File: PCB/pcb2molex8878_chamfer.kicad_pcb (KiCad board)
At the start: 2 copper layers, 16 x 38.2 mm, 2 parts

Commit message: fix pocket dims to account for fitment clearance
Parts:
- gave numbers to parts that had none: 1
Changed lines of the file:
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@@
     (descr "Castellated edge contacts to fit Molex 8878 Socket")
     (solder_mask_margin -0.28)
-    (fp_text reference J? (at -1.5 0 -90) (layer Dwgs.User) hide
+    (fp_text reference m? (at -1.5 0 -90) (layer Dwgs.User) hide
       (effects (font (size 1.2065 1.2065) (thickness 0.127)) (justify left bottom))
     )
@@
       (effects (font (size 1.2065 1.2065) (thickness 0.1016)) (justify left bottom))
     )
+    (fp_line (start 7.2 18.3) (end -7.2 18.3) (layer Dwgs.User) (width 0.01))
+    (fp_line (start 7.2 -18.3) (end 7.2 18.3) (layer Dwgs.User) (width 0.01))
+    (fp_line (start -7.2 -18.3) (end 7.2 -18.3) (layer Dwgs.User) (width 0.01))
+    (fp_line (start -7.2 18.3) (end -7.2 -18.3) (layer Dwgs.User) (width 0.01))
     (fp_text user "backside pocket" (at -4.6 2.85) (layer Dwgs.User)
       (effects (font (size 0.2 0.2) (thickness 0.01)))
     )
-    (fp_text user "36.7 x 14.5 x 1.6" (at -4.6 3.2) (layer Dwgs.User)
+    (fp_text user "36.6 x 14.4 x 1.6" (at -4.6 3.2) (layer Dwgs.User)
       (effects (font (size 0.2 0.2) (thickness 0.01)))
     )
-    (fp_line (start -7.25 3) (end -6 3) (layer Dwgs.User) (width 0.01))
-    (fp_line (start -7.25 3) (end -6.75 3.5) (layer Dwgs.User) (width 0.01))
-    (fp_line (start -7.25 3) (end -6.75 2.5) (layer Dwgs.User) (width 0.01))
-    (fp_line (start 7.25 -18.35) (end 7.25 18.35) (layer Dwgs.User) (width 0.01))
-    (fp_line (start -7.25 -18.35) (end -7.25 18.35) (layer Dwgs.User) (width 0.01))
-    (fp_line (start 7.25 -18.35) (end -7.25 -18.35) (layer Dwgs.User) (width 0.01))
-    (fp_line (start 7.25 18.35) (end -7.25 18.35) (layer Dwgs.User) (width 0.01))
+    (fp_line (start -7.2 3) (end -5.95 3) (layer Dwgs.User) (width 0.01))
+    (fp_line (start -7.2 3) (end -6.7 3.5) (layer Dwgs.User) (width 0.01))
+    (fp_line (start -7.2 3) (end -6.7 2.5) (layer Dwgs.User) (width 0.01))
     (fp_line (start -8 -17.3) (end -6.2 -19.1) (layer Eco2.User) (width 0.01))
     (fp_line (start -8 19.1) (end -8 -17.3) (layer Eco2.User) (width 0.01))

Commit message: show retainer wedges on pcb drawings. add daughterboard in carrier model.
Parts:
- gave numbers to parts that had none: 2
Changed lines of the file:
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@@
     (diff_pair_gap 0.254)
-  )
-  (module 000_LOCAL:pcb2molex8878_chamfer (layer Top)
-    (at 147.2184 99.187)
-    (descr "Castellated edge contacts to fit Molex 8878 Socket")
-    (solder_mask_margin -0.28)
-    (fp_text reference m? (at -1.5 0 -90) (layer Dwgs.User) hide
-      (effects (font (size 1.2065 1.2065) (thickness 0.127)) (justify left bottom))
-    )
-    (fp_text value pcb2molex8878_chamfer (at 2.23 -9.45 -90) (layer F.Fab) hide
-      (effects (font (size 1.2065 1.2065) (thickness 0.1016)) (justify left bottom))
-    )
-    (fp_line (start 7.2 18.3) (end -7.2 18.3) (layer Dwgs.User) (width 0.01))
-    (fp_line (start 7.2 -18.3) (end 7.2 18.3) (layer Dwgs.User) (width 0.01))
-    (fp_line (start -7.2 -18.3) (end 7.2 -18.3) (layer Dwgs.User) (width 0.01))
-    (fp_line (start -7.2 18.3) (end -7.2 -18.3) (layer Dwgs.User) (width 0.01))
-    (fp_text user "backside pocket" (at -4.6 2.85) (layer Dwgs.User)
-      (effects (font (size 0.2 0.2) (thickness 0.01)))
-    )
-    (fp_text user "36.6 x 14.4 x 1.6" (at -4.6 3.2) (layer Dwgs.User)
-      (effects (font (size 0.2 0.2) (thickness 0.01)))
-    )
-    (fp_line (start -7.2 3) (end -5.95 3) (layer Dwgs.User) (width 0.01))
-    (fp_line (start -7.2 3) (end -6.7 3.5) (layer Dwgs.User) (width 0.01))
-    (fp_line (start -7.2 3) (end -6.7 2.5) (layer Dwgs.User) (width 0.01))
-    (fp_line (start -8 -17.3) (end -6.2 -19.1) (layer Eco2.User) (width 0.01))
-    (fp_line (start -8 19.1) (end -8 -17.3) (layer Eco2.User) (width 0.01))
-    (fp_line (start 8 19.1) (end -8 19.1) (layer Eco2.User) (width 0.01))
-    (fp_line (start 8 -19.1) (end 8 19.1) (layer Eco2.User) (width 0.01))
-    (fp_line (start -6.2 -19.1) (end 8 -19.1) (layer Eco2.User) (width 0.01))
-    (fp_line (start -8 -19.1) (end -6.2 -19.1) (layer Dwgs.User) (width 0.01))
-    (fp_line (start -8 -19.1) (end -8 -17.3) (layer Dwgs.User) (width 0.01))
-    (fp_line (start -8 -19.1) (end 8 19.1) (layer Dwgs.User) (width 0.01))
-    (fp_line (start -8 19.1) (end 8 -19.1) (layer Dwgs.User) (width 0.01))
-    (fp_text user "Eco2.User is Edge.Cuts for use with \"pcb2molex8878_chamfer\" carrier." (at -0.05 13.65) (layer Eco2.User)
-      (effects (font (size 0.2 0.2) (thickness 0.01)))
-    )
-    (model ${KIPRJMOD}/000_LOCAL.pretty/3d/pcb2molex8878_chamfer.step
-      (offset (xyz 0 0 -0.4))
-      (scale (xyz 1 1 1))
-      (rotate (xyz 0 0 90))
-    )
   )
   (module 000_LOCAL:pcb2molex8878 locked (layer Top)
@@
     (descr "Castellated edge contacts to fit Molex 8878 Socket")
     (solder_mask_margin -0.28)
-    (fp_text reference J? (at -0.9906 -0.9906 -90) (layer Dwgs.User) hide
+    (fp_text reference contacts1 (at -0.9906 -0.9906 -90) (layer Dwgs.User) hide
       (effects (font (size 1.2065 1.2065) (thickness 0.127)) (justify left bottom))
     )
@@
       (solder_mask_margin -0.19))
   )
+  (module 000_LOCAL:pcb2molex8878_chamfer (layer Top)
+    (at 147.2184 99.187)
+    (descr "Castellated edge contacts to fit Molex 8878 Socket")
+    (solder_mask_margin -0.28)
+    (fp_text reference carrier1 (at -1.5 0 -90) (layer Dwgs.User) hide
+      (effects (font (size 1.2065 1.2065) (thickness 0.127)) (justify left bottom))
+    )
+    (fp_text value pcb2molex8878_chamfer (at 2.23 -9.45 -90) (layer F.Fab) hide
+      (effects (font (size 1.2065 1.2065) (thickness 0.1016)) (justify left bottom))
+    )
+    (fp_text user "10.0 x 1.0 retainer wedges on top surface" (at 0.6 -17.3) (layer Dwgs.User)
+      (effects (font (size 0.2 0.2) (thickness 0.01)))
+    )
+    (fp_line (start -3 -18.1) (end -2.8 -17.9) (layer Dwgs.User) (width 0.01))
+    (fp_line (start -3.2 -17.9) (end -3 -18.1) (layer Dwgs.User) (width 0.01))
+    (fp_line (start -3 -18.1) (end -3.2 -17.9) (layer Dwgs.User) (width 0.01))
+    (fp_line (start -3 -18.1) (end -3 -17.2) (layer Dwgs.User) (width 0.01))
+    (fp_line (start 5 19.1) (end -5 19.1) (layer Dwgs.User) (width 0.01))
+    (fp_line (start 5 18.1) (end 5 19.1) (layer Dwgs.User) (width 0.01))
+    (fp_line (start -5 18.1) (end 5 18.1) (layer Dwgs.User) (width 0.01))
+    (fp_line (start -5 19.1) (end -5 18.1) (layer Dwgs.User) (width 0.01))
+    (fp_line (start 5 -19.1) (end -5 -19.1) (layer Dwgs.User) (width 0.01))
+    (fp_line (start 5 -18.1) (end 5 -19.1) (layer Dwgs.User) (width 0.01))
+    (fp_line (start -5 -18.1) (end 5 -18.1) (layer Dwgs.User) (width 0.01))
+    (fp_line (start -5 -19.1) (end -5 -18.1) (layer Dwgs.User) (width 0.01))
+    (fp_line (start 7.2 18.3) (end -7.2 18.3) (layer Dwgs.User) (width 0.01))
+    (fp_line (start 7.2 -18.3) (end 7.2 18.3) (layer Dwgs.User) (width 0.01))
+    (fp_line (start -7.2 -18.3) (end 7.2 -18.3) (layer Dwgs.User) (width 0.01))
+    (fp_line (start -7.2 18.3) (end -7.2 -18.3) (layer Dwgs.User) (width 0.01))
+    (fp_text user "backside pocket" (at -4.6 2.85) (layer Dwgs.User)
+      (effects (font (size 0.2 0.2) (thickness 0.01)))
+    )
+    (fp_text user "36.6 x 14.4 x 1.6" (at -4.6 3.2) (layer Dwgs.User)
+      (effects (font (size 0.2 0.2) (thickness 0.01)))
+    )
+    (fp_line (start -7.2 3) (end -5.95 3) (layer Dwgs.User) (width 0.01))
+    (fp_line (start -7.2 3) (end -6.7 3.5) (layer Dwgs.User) (width 0.01))
+    (fp_line (start -7.2 3) (end -6.7 2.5) (layer Dwgs.User) (width 0.01))
+    (fp_line (start -8 -17.3) (end -6.2 -19.1) (layer Eco2.User) (width 0.01))
+    (fp_line (start -8 19.1) (end -8 -17.3) (layer Eco2.User) (width 0.01))
+    (fp_line (start 8 19.1) (end -8 19.1) (layer Eco2.User) (width 0.01))
+    (fp_line (start 8 -19.1) (end 8 19.1) (layer Eco2.User) (width 0.01))
+    (fp_line (start -6.2 -19.1) (end 8 -19.1) (layer Eco2.User) (width 0.01))
+    (fp_line (start -8 -19.1) (end -6.2 -19.1) (layer Dwgs.User) (width 0.01))
+    (fp_line (start -8 -19.1) (end -8 -17.3) (layer Dwgs.User) (width 0.01))
+    (fp_line (start -8 -19.1) (end 8 19.1) (layer Dwgs.User) (width 0.01))
+    (fp_line (start -8 19.1) (end 8 -19.1) (layer Dwgs.User) (width 0.01))
+    (fp_text user "Eco2.User is Edge.Cuts for use with \"pcb2molex8878_chamfer\" carrier." (at -0.05 13.65) (layer Eco2.User)
+      (effects (font (size 0.2 0.2) (thickness 0.01)))
+    )
+    (model ${KIPRJMOD}/000_LOCAL.pretty/3d/pcb2molex8878_chamfer.step
+      (offset (xyz 0 0 -0.4))
+      (scale (xyz 1 1 1))
+      (rotate (xyz 0 0 90))
+    )
+  )
   (gr_line (start 139.2184 81.887) (end 139.2184 118.287) (layer Edge.Cuts) (width 0.0254))

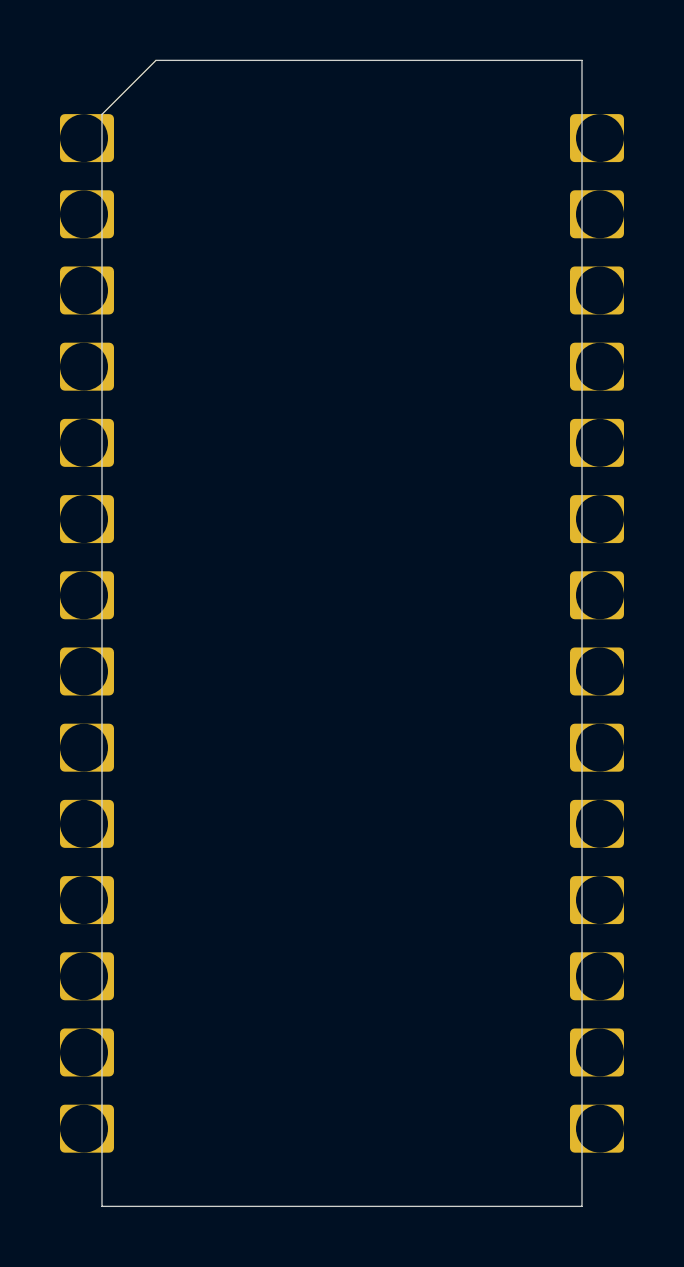
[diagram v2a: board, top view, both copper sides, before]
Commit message: reduce outside X Y dims by 0.1mm for 3d printing variability
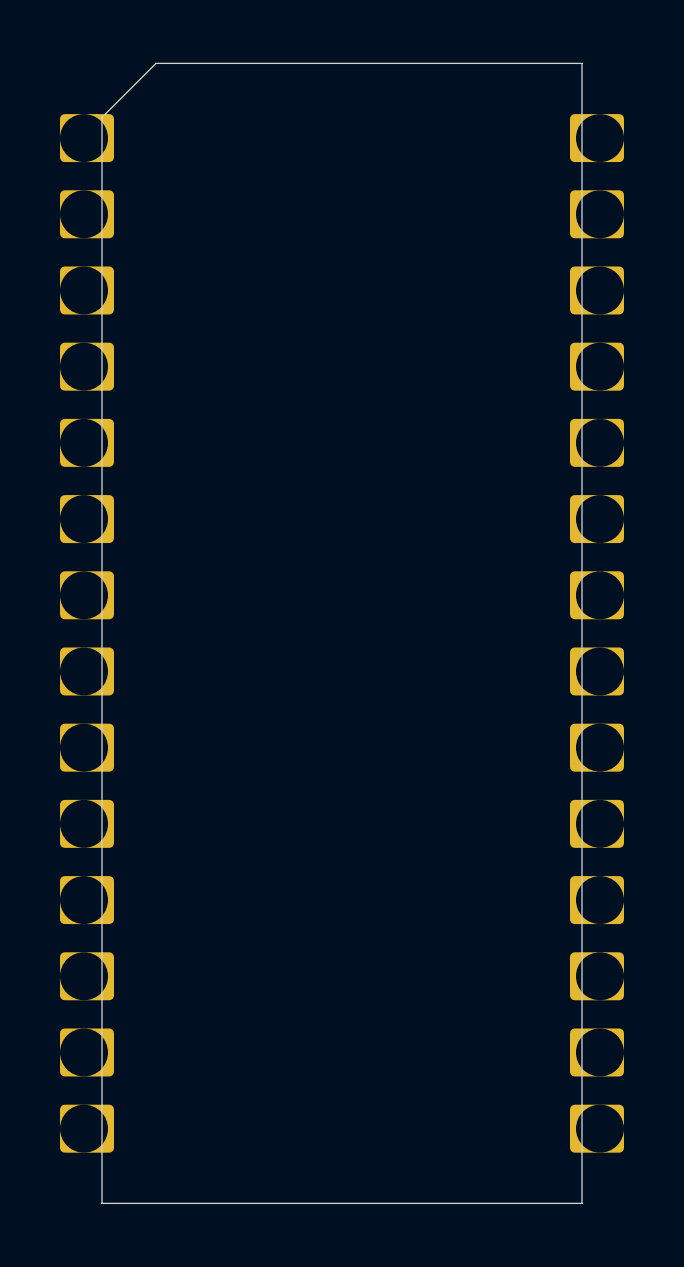
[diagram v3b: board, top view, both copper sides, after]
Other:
- board size 16 x 38.2 mm -> 16 x 38 mm
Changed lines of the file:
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@@
-(kicad_pcb (version 20171130) (host pcbnew 5.1.4-e60b266~84~ubuntu19.04.1)
+(kicad_pcb (version 20171130) (host pcbnew 5.1.5-52549c5~84~ubuntu19.04.1)
   (general
     (thickness 1.6)
@@
     (diff_pair_gap 0.254)
   )
+  (module 000_LOCAL:pcb2molex8878_chamfer (layer Top)
+    (at 147.2184 99.187)
+    (descr "Castellated edge contacts to fit Molex 8878 Socket")
+    (solder_mask_margin -0.28)
+    (fp_text reference carrier1 (at -1.5 0 -90) (layer Dwgs.User) hide
+      (effects (font (size 1.2065 1.2065) (thickness 0.127)) (justify left bottom))
+    )
+    (fp_text value pcb2molex8878_chamfer (at 2.23 -9.45 -90) (layer F.Fab) hide
+      (effects (font (size 1.2065 1.2065) (thickness 0.1016)) (justify left bottom))
+    )
+    (fp_line (start -8 19) (end -8 -17.2) (layer Eco2.User) (width 0.01))
+    (fp_text user "10.0 x 1.0 retainer wedges on top surface" (at 0.6 -17.3) (layer Dwgs.User)
+      (effects (font (size 0.2 0.2) (thickness 0.01)))
+    )
+    (fp_line (start -3 -18) (end -2.8 -17.8) (layer Dwgs.User) (width 0.01))
+    (fp_line (start -3.2 -17.8) (end -3 -18) (layer Dwgs.User) (width 0.01))
+    (fp_line (start -3 -18) (end -3.2 -17.8) (layer Dwgs.User) (width 0.01))
+    (fp_line (start -3 -18) (end -3 -17.1) (layer Dwgs.User) (width 0.01))
+    (fp_line (start 5 19) (end -5 19) (layer Dwgs.User) (width 0.01))
+    (fp_line (start 5 18) (end 5 19) (layer Dwgs.User) (width 0.01))
+    (fp_line (start -5 18) (end 5 18) (layer Dwgs.User) (width 0.01))
+    (fp_line (start -5 19) (end -5 18) (layer Dwgs.User) (width 0.01))
+    (fp_line (start 5 -19) (end -5 -19) (layer Dwgs.User) (width 0.01))
+    (fp_line (start 5 -18) (end 5 -19) (layer Dwgs.User) (width 0.01))
+    (fp_line (start -5 -18) (end 5 -18) (layer Dwgs.User) (width 0.01))
+    (fp_line (start -5 -19) (end -5 -18) (layer Dwgs.User) (width 0.01))
+    (fp_line (start 7.2 18.3) (end -7.2 18.3) (layer Dwgs.User) (width 0.01))
+    (fp_line (start 7.2 -18.3) (end 7.2 18.3) (layer Dwgs.User) (width 0.01))
+    (fp_line (start -7.2 -18.3) (end 7.2 -18.3) (layer Dwgs.User) (width 0.01))
+    (fp_line (start -7.2 18.3) (end -7.2 -18.3) (layer Dwgs.User) (width 0.01))
+    (fp_text user "backside pocket" (at -4.6 2.85) (layer Dwgs.User)
+      (effects (font (size 0.2 0.2) (thickness 0.01)))
+    )
+    (fp_text user "36.6 x 14.4 x 1.6" (at -4.6 3.2) (layer Dwgs.User)
+      (effects (font (size 0.2 0.2) (thickness 0.01)))
+    )
+    (fp_line (start -7.2 3) (end -5.95 3) (layer Dwgs.User) (width 0.01))
+    (fp_line (start -7.2 3) (end -6.7 3.5) (layer Dwgs.User) (width 0.01))
+    (fp_line (start -7.2 3) (end -6.7 2.5) (layer Dwgs.User) (width 0.01))
+    (fp_line (start -8 -17.2) (end -6.2 -19) (layer Eco2.User) (width 0.01))
+    (fp_line (start 8 19) (end -8 19) (layer Eco2.User) (width 0.01))
+    (fp_line (start 8 -19) (end 8 19) (layer Eco2.User) (width 0.01))
+    (fp_line (start -6.2 -19) (end 8 -19) (layer Eco2.User) (width 0.01))
+    (fp_line (start -8 -19) (end -6.2 -19) (layer Dwgs.User) (width 0.01))
+    (fp_line (start -8 -19) (end -8 -17.2) (layer Dwgs.User) (width 0.01))
+    (fp_text user "Eco2.User is Edge.Cuts for use with \"pcb2molex8878_chamfer\" carrier." (at -0.05 13.65) (layer Eco2.User)
+      (effects (font (size 0.2 0.2) (thickness 0.01)))
+    )
+    (model ${KIPRJMOD}/000_LOCAL.pretty/3d/pcb2molex8878_chamfer.step
+      (offset (xyz 0 0 -0.4))
+      (scale (xyz 1 1 1))
+      (rotate (xyz 0 0 90))
+    )
+  )
   (module 000_LOCAL:pcb2molex8878 locked (layer Top)
     (at 147.2184 99.187)
@@
       (solder_mask_margin -0.19))
   )
-  (module 000_LOCAL:pcb2molex8878_chamfer (layer Top)
-    (at 147.2184 99.187)
-    (descr "Castellated edge contacts to fit Molex 8878 Socket")
-    (solder_mask_margin -0.28)
-    (fp_text reference carrier1 (at -1.5 0 -90) (layer Dwgs.User) hide
-      (effects (font (size 1.2065 1.2065) (thickness 0.127)) (justify left bottom))
-    )
-    (fp_text value pcb2molex8878_chamfer (at 2.23 -9.45 -90) (layer F.Fab) hide
-      (effects (font (size 1.2065 1.2065) (thickness 0.1016)) (justify left bottom))
-    )
-    (fp_text user "10.0 x 1.0 retainer wedges on top surface" (at 0.6 -17.3) (layer Dwgs.User)
-      (effects (font (size 0.2 0.2) (thickness 0.01)))
-    )
-    (fp_line (start -3 -18.1) (end -2.8 -17.9) (layer Dwgs.User) (width 0.01))
-    (fp_line (start -3.2 -17.9) (end -3 -18.1) (layer Dwgs.User) (width 0.01))
-    (fp_line (start -3 -18.1) (end -3.2 -17.9) (layer Dwgs.User) (width 0.01))
-    (fp_line (start -3 -18.1) (end -3 -17.2) (layer Dwgs.User) (width 0.01))
-    (fp_line (start 5 19.1) (end -5 19.1) (layer Dwgs.User) (width 0.01))
-    (fp_line (start 5 18.1) (end 5 19.1) (layer Dwgs.User) (width 0.01))
-    (fp_line (start -5 18.1) (end 5 18.1) (layer Dwgs.User) (width 0.01))
-    (fp_line (start -5 19.1) (end -5 18.1) (layer Dwgs.User) (width 0.01))
-    (fp_line (start 5 -19.1) (end -5 -19.1) (layer Dwgs.User) (width 0.01))
-    (fp_line (start 5 -18.1) (end 5 -19.1) (layer Dwgs.User) (width 0.01))
-    (fp_line (start -5 -18.1) (end 5 -18.1) (layer Dwgs.User) (width 0.01))
-    (fp_line (start -5 -19.1) (end -5 -18.1) (layer Dwgs.User) (width 0.01))
-    (fp_line (start 7.2 18.3) (end -7.2 18.3) (layer Dwgs.User) (width 0.01))
-    (fp_line (start 7.2 -18.3) (end 7.2 18.3) (layer Dwgs.User) (width 0.01))
-    (fp_line (start -7.2 -18.3) (end 7.2 -18.3) (layer Dwgs.User) (width 0.01))
-    (fp_line (start -7.2 18.3) (end -7.2 -18.3) (layer Dwgs.User) (width 0.01))
-    (fp_text user "backside pocket" (at -4.6 2.85) (layer Dwgs.User)
-      (effects (font (size 0.2 0.2) (thickness 0.01)))
-    )
-    (fp_text user "36.6 x 14.4 x 1.6" (at -4.6 3.2) (layer Dwgs.User)
-      (effects (font (size 0.2 0.2) (thickness 0.01)))
-    )
-    (fp_line (start -7.2 3) (end -5.95 3) (layer Dwgs.User) (width 0.01))
-    (fp_line (start -7.2 3) (end -6.7 3.5) (layer Dwgs.User) (width 0.01))
-    (fp_line (start -7.2 3) (end -6.7 2.5) (layer Dwgs.User) (width 0.01))
-    (fp_line (start -8 -17.3) (end -6.2 -19.1) (layer Eco2.User) (width 0.01))
-    (fp_line (start -8 19.1) (end -8 -17.3) (layer Eco2.User) (width 0.01))
-    (fp_line (start 8 19.1) (end -8 19.1) (layer Eco2.User) (width 0.01))
-    (fp_line (start 8 -19.1) (end 8 19.1) (layer Eco2.User) (width 0.01))
-    (fp_line (start -6.2 -19.1) (end 8 -19.1) (layer Eco2.User) (width 0.01))
-    (fp_line (start -8 -19.1) (end -6.2 -19.1) (layer Dwgs.User) (width 0.01))
-    (fp_line (start -8 -19.1) (end -8 -17.3) (layer Dwgs.User) (width 0.01))
-    (fp_line (start -8 -19.1) (end 8 19.1) (layer Dwgs.User) (width 0.01))
-    (fp_line (start -8 19.1) (end 8 -19.1) (layer Dwgs.User) (width 0.01))
-    (fp_text user "Eco2.User is Edge.Cuts for use with \"pcb2molex8878_chamfer\" carrier." (at -0.05 13.65) (layer Eco2.User)
-      (effects (font (size 0.2 0.2) (thickness 0.01)))
-    )
-    (model ${KIPRJMOD}/000_LOCAL.pretty/3d/pcb2molex8878_chamfer.step
-      (offset (xyz 0 0 -0.4))
-      (scale (xyz 1 1 1))
-      (rotate (xyz 0 0 90))
-    )
-  )
-  (gr_line (start 139.2184 81.887) (end 139.2184 118.287) (layer Edge.Cuts) (width 0.0254))
-  (gr_line (start 141.0184 80.087) (end 139.2184 81.887) (layer Edge.Cuts) (width 0.0254))
-  (gr_line (start 155.2184 80.087) (end 141.0184 80.087) (layer Edge.Cuts) (width 0.0254))
-  (gr_line (start 155.2184 118.287) (end 155.2184 80.087) (layer Edge.Cuts) (width 0.0254))
-  (gr_line (start 139.2184 118.287) (end 155.2184 118.287) (layer Edge.Cuts) (width 0.0254))
+  (gr_line (start 155.2184 80.187) (end 155.2184 118.187) (layer Edge.Cuts) (width 0.0254))
+  (gr_line (start 139.2184 118.187) (end 139.2184 81.987) (layer Edge.Cuts) (width 0.0254))
+  (gr_line (start 141.0184 80.187) (end 139.2184 81.987) (layer Edge.Cuts) (width 0.0254))
+  (gr_line (start 155.2184 80.187) (end 141.0184 80.187) (layer Edge.Cuts) (width 0.0254))
+  (gr_line (start 139.2184 118.187) (end 155.2184 118.187) (layer Edge.Cuts) (width 0.0254))
 )
